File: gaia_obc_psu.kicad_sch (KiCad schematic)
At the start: 73 parts, among them IC1 MAX17048G+T10, J4 Conn_01x02_Pin, Q1 FS8205A, U10 TPS22917DBV, U11 AP2112K-3.3, U12 DW01A, U13 AP2112K-3.0, U14 LGS4056HDB, U4 INA3221, U5 INA3221, U6 TPS22917DBV, U7 TPS22917DBV, U8 TPS22917DBV, U9 TPS22917DBV

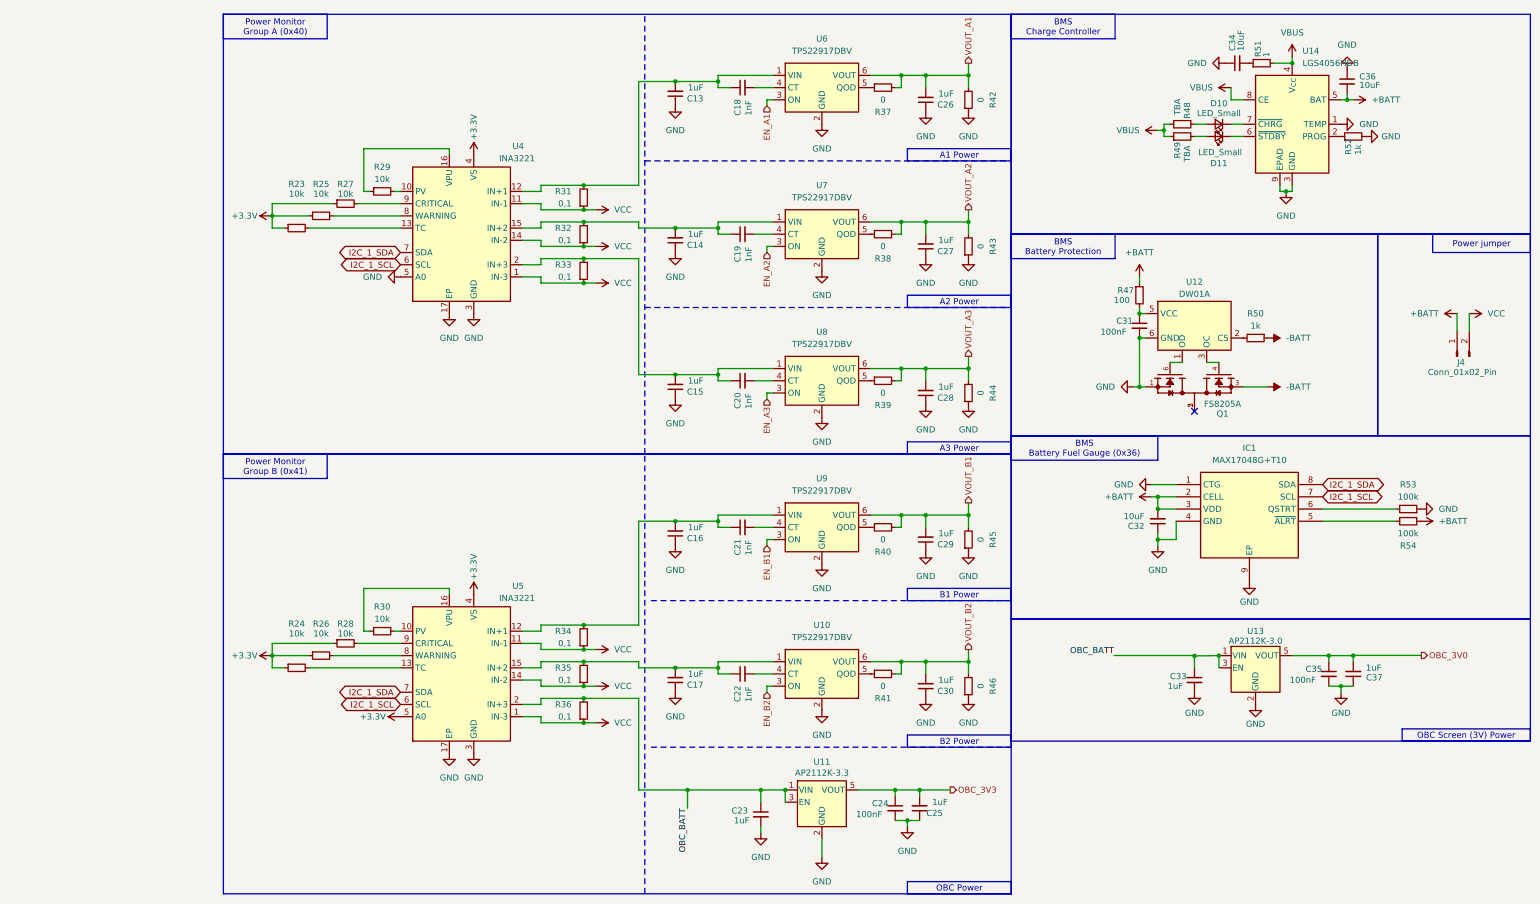
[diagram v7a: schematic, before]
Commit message: Finalizing schematic+Start placing components
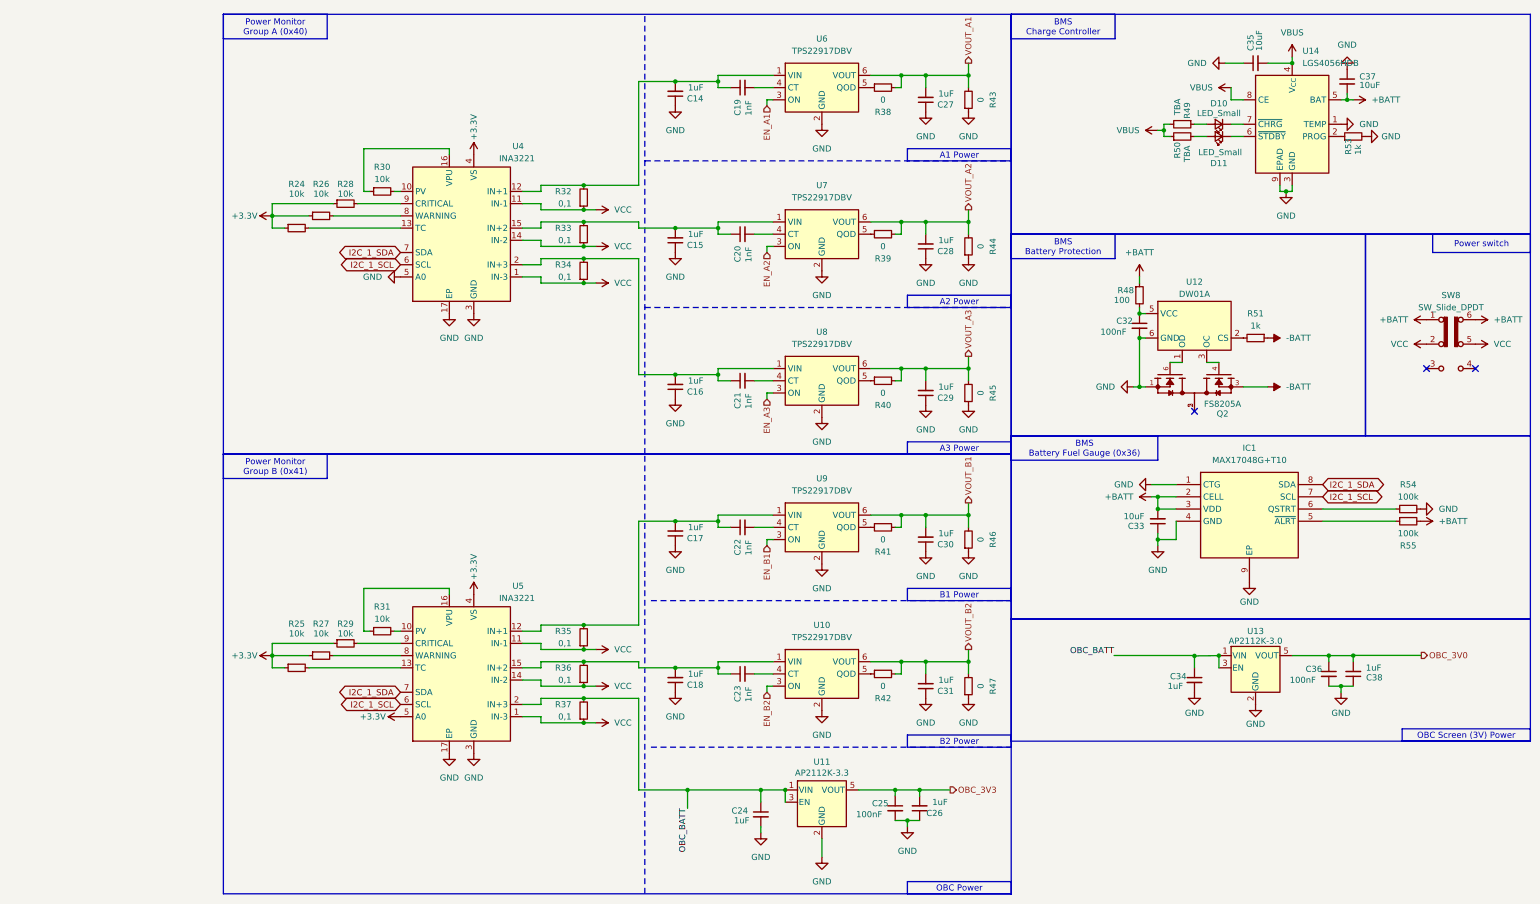
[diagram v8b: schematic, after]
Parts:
- removed J4: Conn_01x02_Pin, Connector_Molex:Molex_MicroClasp_55935-0230_1x02_P2.00mm_Horizontal, symbol Connector:Conn_01x02_Pin
- removed R51: 1, Resistor_SMD:R_0603_1608Metric, symbol Device:R_Small
- added SW8: SW_Slide_DPDT, gaia_obc-footprints:MS-22D28-G020, symbol Switch:SW_Slide_DPDT
- R48: renamed from R47; footprint Resistor_SMD:R_1206_3216Metric -> Resistor_SMD:R_0603_1608Metric
- R53: renamed from R52; footprint Resistor_SMD:R_0603_1608Metric -> Resistor_SMD:R_0402_1005Metric
- renumbered C13 to C14, C14 to C15, C15 to C16, C16 to C17, C17 to C18, C18 to C19, C19 to C20, C20 to C21, C21 to C22, C22 to C23, C23 to C24, C24 to C25, C25 to C26, C26 to C27, C27 to C28, C28 to C29, C29 to C30, C30 to C31, C31 to C32, C32 to C33, C33 to C34, C34 to C35, C35 to C36, C36 to C37, C37 to C38, Q1 to Q2, R23 to R24, R24 to R25, R25 to R26, R26 to R27, R27 to R28, R28 to R29, R29 to R30, R30 to R31, R31 to R32, R32 to R33, R33 to R34, R34 to R35, R35 to R36, R36 to R37, R37 to R38, R38 to R39, R39 to R40, R40 to R41, R41 to R42, R42 to R43, R43 to R44, R44 to R45, R45 to R46, R46 to R47, R48 to R49, R49 to R50, R50 to R51, R53 to R54, R54 to R55
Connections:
- net +BATT: now also SW8.1 (A), SW8.6 (C)
- net VBUS: now also C35.2
- net VCC: now also SW8.2 (B), SW8.5 (B)
- no-connect marks 1 -> 3
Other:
- moved on the sheet: C35
